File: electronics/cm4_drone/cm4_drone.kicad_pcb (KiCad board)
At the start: 4 copper layers, 69.2 x 40 mm, 55 parts, among them J8 Conn_01x02_Female, J9 Conn_01x02_Female, U1 74LVC1G04, U3 ADS1115IDGS, U5 Compute_Module_4_Connectors

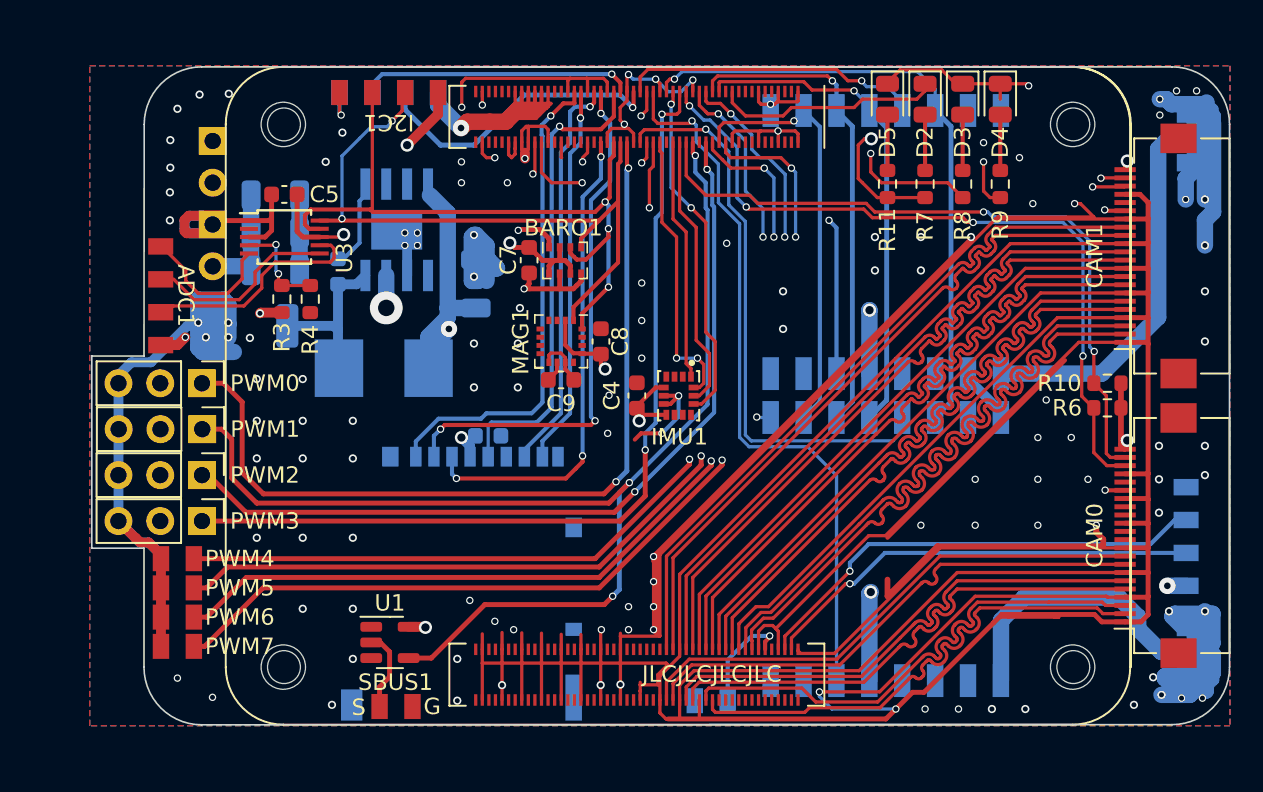
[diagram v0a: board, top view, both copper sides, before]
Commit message: wip new pcb with m2 connector
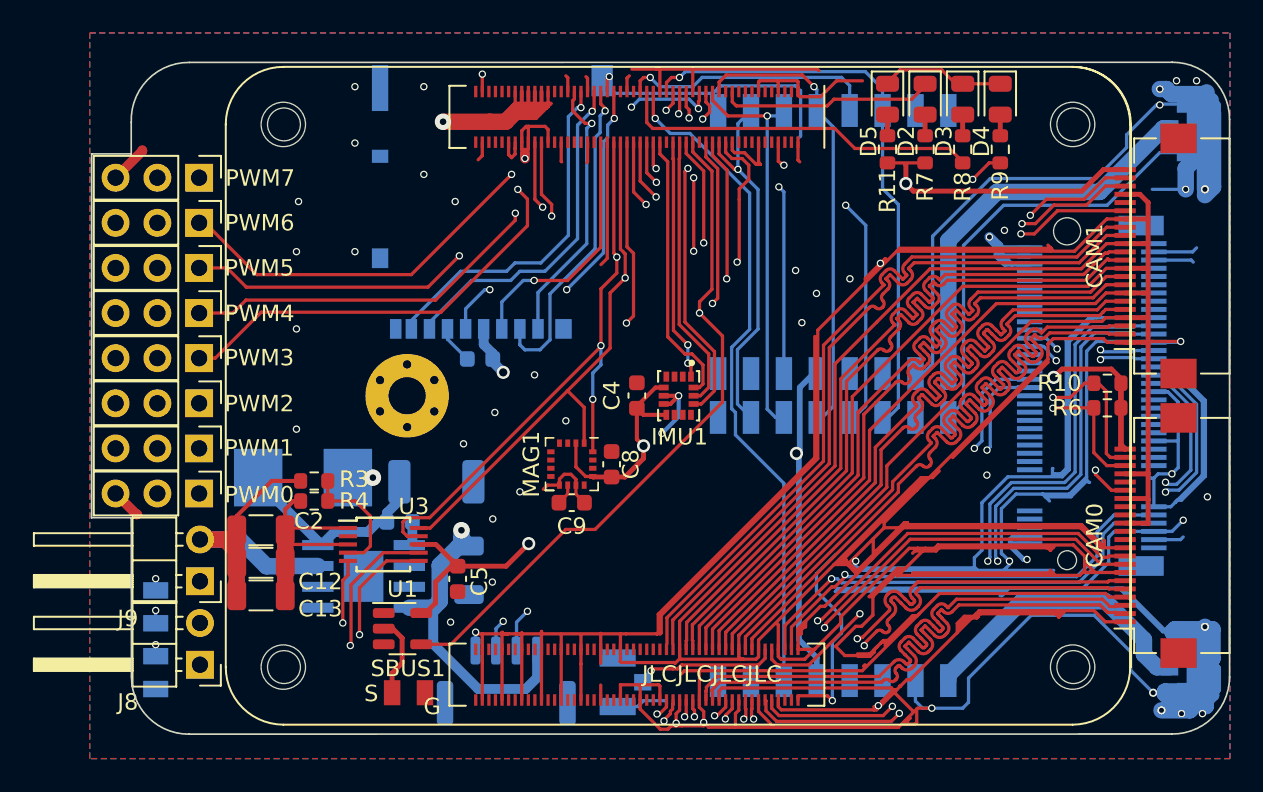
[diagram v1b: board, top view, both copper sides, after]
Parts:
- removed BARO1: BMP280, Package_LGA:Bosch_LGA-8_2x2.5mm_P0.65mm_ClockwisePinNumbering
- removed C7: 100nF, Capacitor_SMD:C_0603_1608Metric
- removed I2C1, UART0: Conn_01x04_Female, cm4_drone:Breakout_1x04_2mm_SMD
- added J3: Bus_M.2_Socket_B, footprints:AMPHENOL_MDT420B03002, B.Cu at (23.6, 0.00)
- added REF**: VAL**, conn-wire-pads:Hole-Screw-#2, F.Cu at (-16.5, 0.00)
- ADC1: moved to B.Cu
- C12, C13, C2, J8, J9: moved to F.Cu
- PWM4, PWM5, PWM6, PWM7: value Conn_01x02_Female -> Conn_01x03_Female; footprint cm4_drone:Breakout_1x02_2mm_SMD -> Connector_PinHeader_2.54mm:PinHeader_1x03_P2.54mm_Vertical
- TV1: footprint cm4_drone:Breakout_1x02_2mm_SMD -> Connector_Coaxial:U.FL_Hirose_U.FL-R-SMT-1_Vertical
- USB1: footprint cm4_drone:Breakout_1x04_2mm_SMD -> Connector_JST:JST_GH_SM04B-GHS-TB_1x04-1MP_P1.25mm_Horizontal
- moved USB1 42.3 mm to (-10.5, 17.3), turned to 180 degrees
- moved J8 31.9 mm to (-29.1, 16.4)
- moved PWM7 28.5 mm to (-29.2, -13.3), turned to -90 degrees
- moved C5 25.6 mm to (-13.4, 11.1), turned to 90 degrees
- moved PWM6 24.0 mm to (-29.2, -10.5), turned to -90 degrees
- moved SD1 23.3 mm to (-11.3, -11.8), turned to 0 degrees
- moved J9 21.7 mm to (-29.1, 11.3)
- moved DC1 21.2 mm to (-19.2, 11.0), turned to 180 degrees
- moved ADC1 20.9 mm to (-31.8, 14.8)
- moved C2 20.4 mm to (-25.4, 8.18)
- moved C12 20.1 mm to (-25.4, 10.2)
- moved C13 19.8 mm to (-25.4, 12.1)
- moved U3 19.6 mm to (-18.0, 9.04)
- moved PWM5 19.5 mm to (-29.2, -7.77), turned to -90 degrees
- moved C6 17.4 mm to (-12.8, 10.6), turned to -90 degrees
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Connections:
- PWM4 pad 2: GND -> unconnected-(PWM4-Pad2)
- PWM5 pad 2: GND -> unconnected-(PWM5-Pad2)
- PWM6 pad 2: GND -> unconnected-(PWM6-Pad2)
- PWM7 pad 2: GND -> unconnected-(PWM7-Pad2)
- RADIO2 pad 16: unconnected-(RADIO2-Pad16) -> GND
- TV1 pad 1: GND -> TVOUT
- TV1 pad 2: TVOUT -> GND
- U5 pad 102: unconnected-(U5-Pad102) -> PCIe_REQ
- U5 pad 108: unconnected-(U5-Pad108) -> GND
- U5 pad 109: unconnected-(U5-Pad109) -> PCIe_RST
- U5 pad 110: unconnected-(U5-Pad110) -> PCIe_CLK_P
- U5 pad 112: unconnected-(U5-Pad112) -> PCIe_CLK_N
- U5 pad 114: unconnected-(U5-Pad114) -> GND
- U5 pad 116: unconnected-(U5-Pad116) -> PCIe_RX_P
- U5 pad 118: unconnected-(U5-Pad118) -> PCIe_RX_N
- U5 pad 120: unconnected-(U5-Pad120) -> GND
- U5 pad 122: unconnected-(U5-Pad122) -> PCIe_TX_P
- U5 pad 124: unconnected-(U5-Pad124) -> PCIe_TX_N
- U5 pad 126: unconnected-(U5-Pad126) -> GND
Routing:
- net GND: track 744.4 -> 1277.4 mm, vias 131 -> 49
- net PCIe_REQ: track 0.00 -> 47.3 mm, vias 0 -> 2
- net PCIe_TX_P: track 0.00 -> 47.2 mm, vias 0 -> 2
- net PCIe_TX_N: track 0.00 -> 47.2 mm, vias 0 -> 2
- net PCIe_CLK_N: track 0.00 -> 47.0 mm, vias 0 -> 2
- net PCIe_RX_P: track 0.00 -> 47.0 mm, vias 0 -> 2
- net PCIe_CLK_P: track 0.00 -> 46.9 mm, vias 0 -> 2
- net PCIe_RX_N: track 0.00 -> 46.9 mm, vias 0 -> 2
- net 5V: track 132.2 -> 92.5 mm
- net PCIe_RST: track 0.00 -> 36.1 mm, vias 0 -> 2
- net 3.3V: track 0.00 -> 34.9 mm, vias 0 -> 3
- net I2C1_SDA: track 43.8 -> 70.8 mm, vias 3 -> 4
- net CM4_3.3V: track 56.8 -> 82.0 mm, vias 13 -> 9
- net SOFT_PWM6: track 62.7 -> 37.8 mm, vias 3 -> 2
- net USB2_D-: track 26.8 -> 50.5 mm, vias 1 -> 2
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- added copper zone on In1.Cu, net GND
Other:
- board size 69.2 x 40 mm -> 69.2 x 40.9 mm
